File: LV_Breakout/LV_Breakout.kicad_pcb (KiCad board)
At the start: 2 copper layers, 116.8 x 64.8 mm, 17 parts, among them J1 LOGIC_PWR, J2 GLV_IN, J4 BMS, J5 DAQ, J6 DAQ_AMPSEAL, J7 PWR_AMPSEAL, K1 RAYEX-L90B

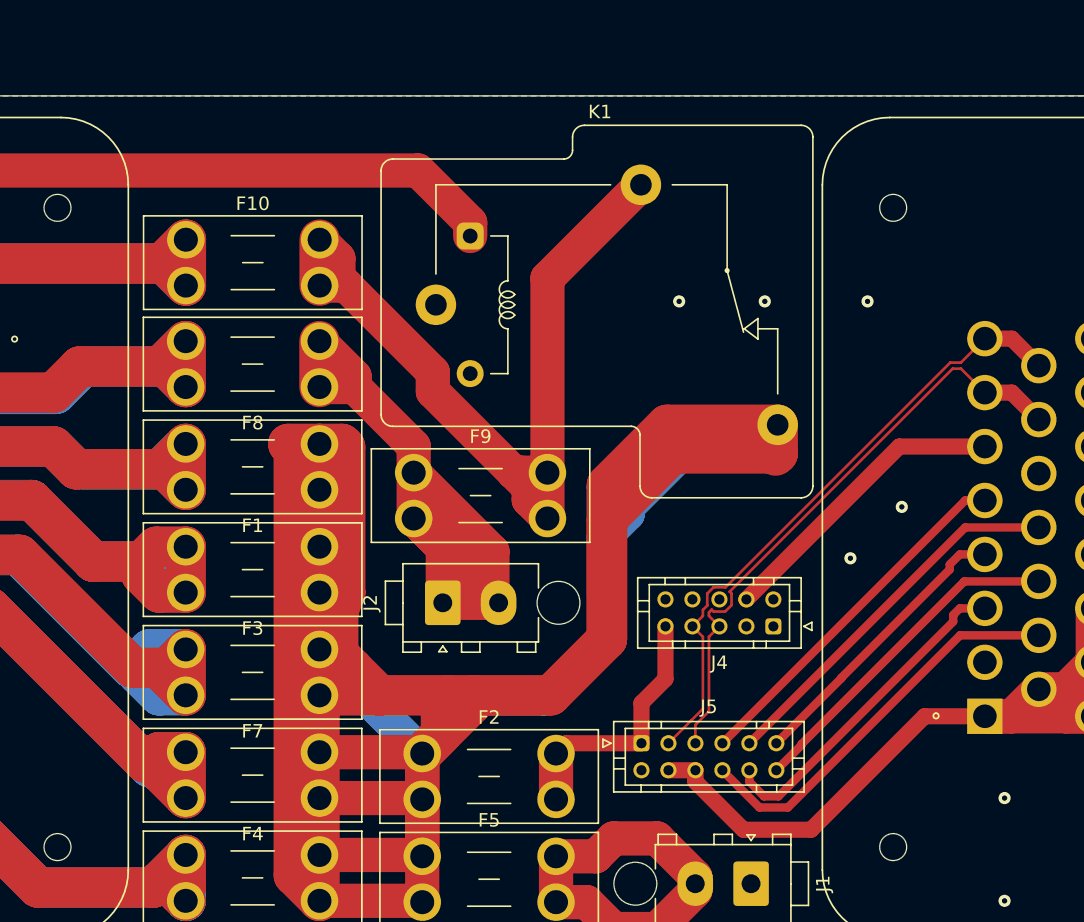
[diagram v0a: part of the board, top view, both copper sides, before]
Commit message: Footprint updates of GLV board, pull the libraries repo please!
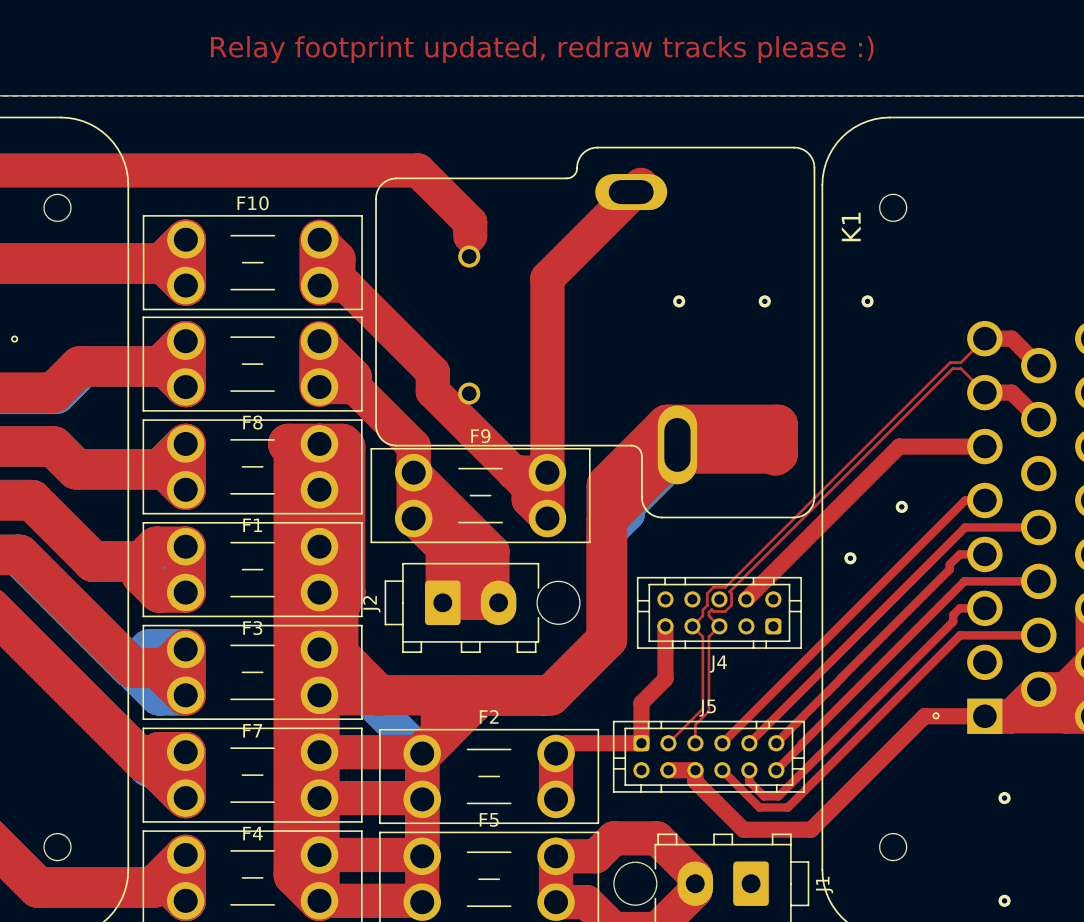
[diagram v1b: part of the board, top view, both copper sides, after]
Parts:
- F1, F10, F2, F3, F4, F5, F6, F7, F8, F9: footprint Fuse:Fuseholder_Blade_Mini_Keystone_3568 -> AERO-footprints:Fuseholder_Blade_Mini_Keystone_3568
- J1, J2: footprint aero_footprint:TE_MATE-N-LOK_1-770866-x_1x02_P4.14mm_Vertical -> AERO-footprints:TE_MATE-N-LOK_1-770866-x_1x02_P4.14mm_Vertical
- J4: footprint Connector_JST:JST_PHD_B10B-PHDSS_2x05_P2.00mm_Vertical -> AERO-footprints:JST_PHD_B10B-PHDSS_2x05_P2.00mm_Vertical
- J5: footprint Connector_JST:JST_PHD_B12B-PHDSS_2x06_P2.00mm_Vertical -> AERO-footprints:JST_PHD_B12B-PHDSS_2x06_P2.00mm_Vertical
- J6, J7: footprint aero_footprint:TE_1-776200-1_23pin_Vertical -> AERO-footprints:TE_1-776200-1_23pin_Vertical
- K1: value RAYEX-L90B -> T9VV1K15-12S; footprint Relay_THT:Relay_SPST_RAYEX-L90B -> AERO-footprints:RELAY_T9VV1K15-12S
- moved K1 14.5 mm to (194.6, 22.9), turned to 270 degrees
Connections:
- J4 pad 1: (no net) -> /USB_GND
- J4 pad 2: (no net) -> /USB+
- J4 pad 3: (no net) -> /USB-
- J4 pad 6: (no net) -> /USB_5V
- J4 pad 8: (no net) -> Net-(J4-Pad8)
- J6 pad 13: (no net) -> Net-(J6-Pad13)
- J6 pad 2: (no net) -> /SENSOR_7
- J7 pad 1: (no net) -> Net-(J7-Pad1)
- J7 pad 17: (no net) -> Net-(J7-Pad17)
- J7 pad 18: (no net) -> Net-(J7-Pad18)
- J7 pad 7: (no net) -> Net-(J7-Pad7)
- J7 pad 8: (no net) -> Net-(J7-Pad8)
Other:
- board text added: "Relay footprint updated, redraw tracks please :)"

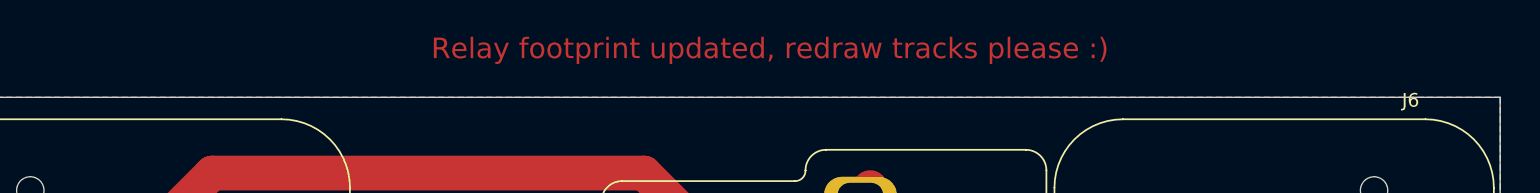
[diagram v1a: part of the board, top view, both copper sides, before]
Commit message: Final fixes to GLV board so it works with HV board
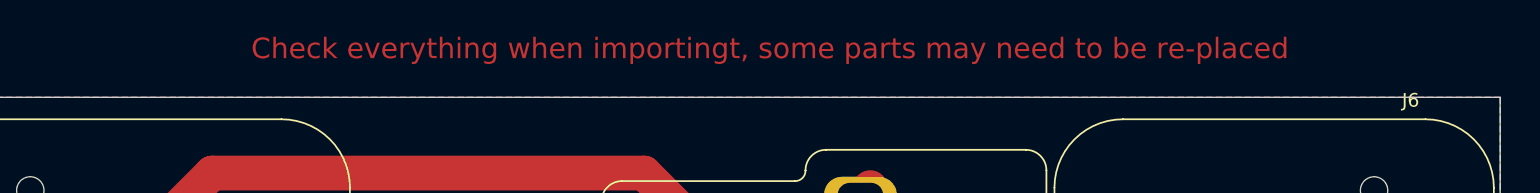
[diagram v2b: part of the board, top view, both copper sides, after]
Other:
- board text added: "Check everything when importingt, some parts may need to be re-placed"
- board text removed: "Relay footprint updated, redraw tracks please :)"

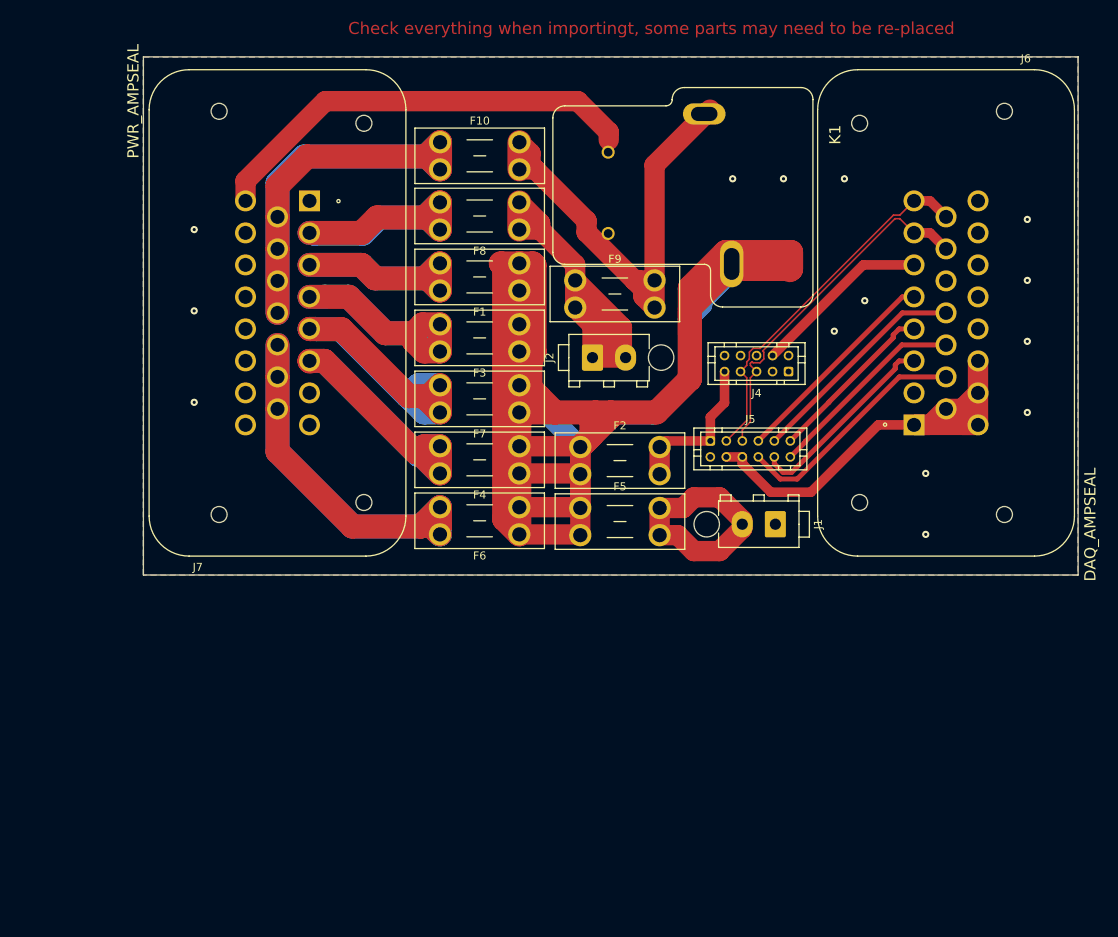
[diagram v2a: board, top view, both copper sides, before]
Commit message: LVPDU schem and pcb
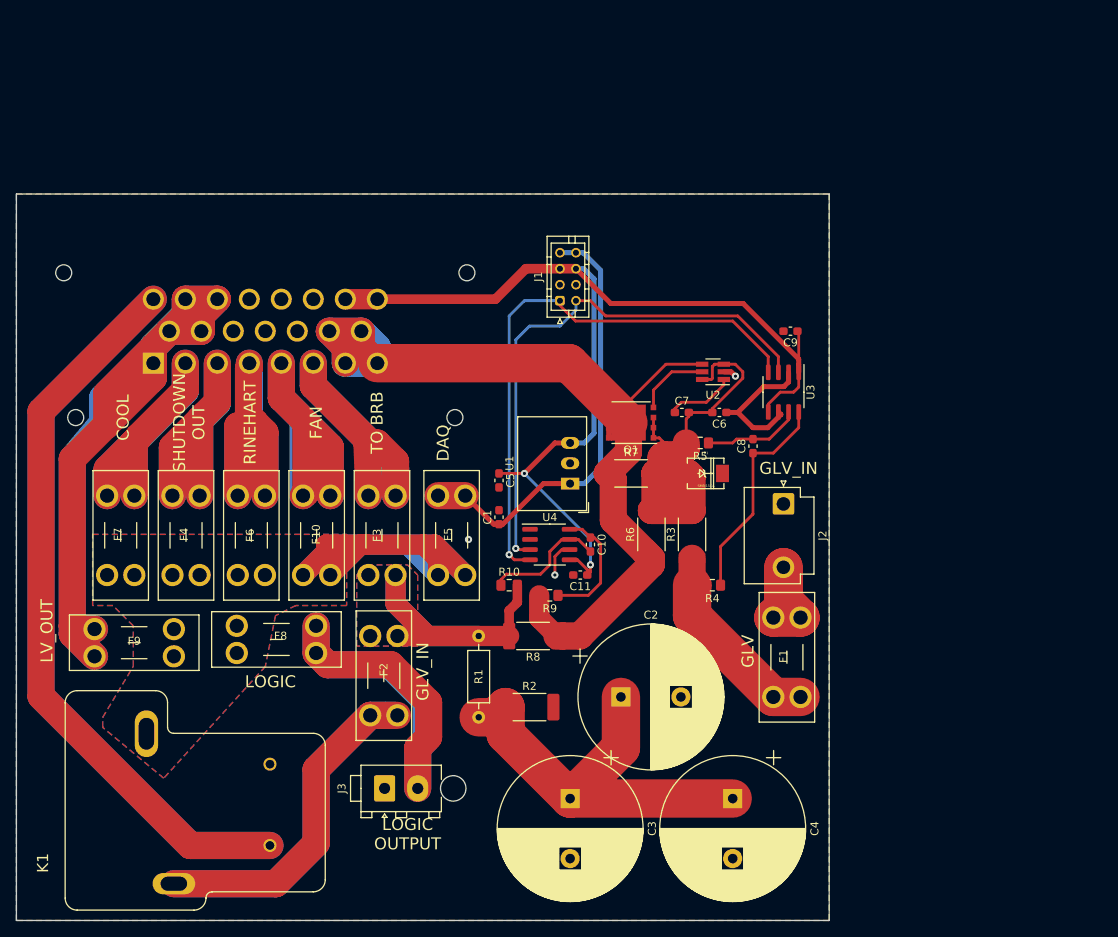
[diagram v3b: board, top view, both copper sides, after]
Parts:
- removed J5: DAQ, AERO-footprints:JST_PHD_B12B-PHDSS_2x06_P2.00mm_Vertical
- removed J6: DAQ_AMPSEAL, AERO-footprints:TE_1-776200-1_23pin_Vertical
- removed J7: PWR_AMPSEAL, AERO-footprints:TE_1-776200-1_23pin_Vertical
- added C1: 1u, Capacitor_SMD:C_0603_1608Metric_Pad1.05x0.95mm_HandSolder, F.Cu at (168.9, 63.9)
- added C10: 1uF, Capacitor_SMD:C_0603_1608Metric_Pad1.05x0.95mm_HandSolder, F.Cu at (180.3, 67.3)
- added C11: 0.1uF, Capacitor_SMD:C_0603_1608Metric_Pad1.05x0.95mm_HandSolder, F.Cu at (179.1, 71.1)
- added C2: URS1E472MHD, Capacitor_THT:CP_Radial_D18.0mm_P7.50mm, F.Cu at (184.2, 86.4)
- added C3: URS1E472MHD, Capacitor_THT:CP_Radial_D18.0mm_P7.50mm, F.Cu at (177.8, 99.1)
- added C4: URS1E472MHD, Capacitor_THT:CP_Radial_D18.0mm_P7.50mm, F.Cu at (198.1, 99.1)
- added C5: 10u, Capacitor_SMD:C_0603_1608Metric_Pad1.05x0.95mm_HandSolder, F.Cu at (168.9, 59.3)
- added C6: 22nF, Capacitor_SMD:C_0603_1608Metric_Pad1.05x0.95mm_HandSolder, F.Cu at (196.5, 50.8)
- added C7: 0.1uF, Capacitor_SMD:C_0603_1608Metric_Pad1.05x0.95mm_HandSolder, F.Cu at (191.8, 50.8)
- added C8: 1uF, Capacitor_SMD:C_0603_1608Metric_Pad1.05x0.95mm_HandSolder, F.Cu at (200.7, 55.0)
- added C9: 0.1uF, Capacitor_SMD:C_0603_1608Metric_Pad1.05x0.95mm_HandSolder, F.Cu at (205.3, 40.6)
- added D1: SMBJ15CA, AERO_FOOT:DO-214AA, F.Cu at (194.7, 58.4)
- added G***: LOGO, AERO_CUSTOM:AERO_Logo_15x6mm, B.Cu at (195.6, 31.8)
- added J3: TE 1-770872-0, AERO_CUSTOM:TE_MATE-N-LOK_1-770866-x_1x02_P4.14mm_Vertical, F.Cu at (154.6, 97.8)
- added Q1: CSD18563Q5A, Package_SON:VSONP-8-1EP_5x6_P1.27mm, F.Cu at (185.4, 52.1)
- added R1: RR01J2R0TB, Resistor_THT:R_Axial_DIN0207_L6.3mm_D2.5mm_P10.16mm_Horizontal, F.Cu at (166.4, 88.9)
- added R10: 10, Resistor_SMD:R_0805_2012Metric_Pad1.15x1.40mm_HandSolder, F.Cu at (170.2, 72.4)
- added R2: 50M, Resistor_SMD:R_2512_6332Metric_Pad1.52x3.35mm_HandSolder, F.Cu at (172.7, 87.6)
- added R3: KRL6432E-M-R003-F-T1, Resistor_SMD:R_2512_6332Metric_Pad1.52x3.35mm_HandSolder, F.Cu at (193.0, 66.0)
- added R4: 10, Resistor_SMD:R_0805_2012Metric_Pad1.15x1.40mm_HandSolder, F.Cu at (195.6, 72.4)
- added R5: 10, Resistor_SMD:R_0805_2012Metric_Pad1.15x1.40mm_HandSolder, F.Cu at (194.1, 54.6)
- added R6: 20, Resistor_SMD:R_2512_6332Metric_Pad1.52x3.35mm_HandSolder, F.Cu at (188.0, 66.0)
- added R7: 20, Resistor_SMD:R_2512_6332Metric_Pad1.52x3.35mm_HandSolder, F.Cu at (185.4, 58.4)
- added R8: KRL6432E-M-R003-F-T1, Resistor_SMD:R_2512_6332Metric_Pad1.52x3.35mm_HandSolder, F.Cu at (173.2, 78.7)
- added R9: 10, Resistor_SMD:R_0805_2012Metric_Pad1.15x1.40mm_HandSolder, F.Cu at (175.3, 73.7)
- added U1: R-78E5.0-0.5, Converter_DCDC:Converter_DCDC_RECOM_R-78E-0.5_THT, F.Cu at (177.8, 59.7)
- added U2: LM74700QDBVTQ1, Package_TO_SOT_SMD:SOT-23-6_Handsoldering, F.Cu at (195.7, 45.7)
- added U3: INA219AIDR, Package_SO:SOIC-8_3.9x4.9mm_P1.27mm, F.Cu at (204.5, 48.3)
- added U4: INA219AIDR, Package_SO:SOIC-8_3.9x4.9mm_P1.27mm, F.Cu at (175.3, 67.3)
- F1: value SHUTDOWN -> 3568 Mini Blade; footprint AERO-footprints:Fuseholder_Blade_Mini_Keystone_3568 -> AERO_FOOT:Fuseholder_Blade_Mini_Keystone_3568
- F10: value DCDC -> 3568 Mini Blade; footprint AERO-footprints:Fuseholder_Blade_Mini_Keystone_3568 -> AERO_FOOT:Fuseholder_Blade_Mini_Keystone_3568
- F2: value BMS -> 3568 Mini Blade; footprint AERO-footprints:Fuseholder_Blade_Mini_Keystone_3568 -> AERO_FOOT:Fuseholder_Blade_Mini_Keystone_3568
- F3: value RINEHART -> 3568 Mini Blade; footprint AERO-footprints:Fuseholder_Blade_Mini_Keystone_3568 -> AERO_FOOT:Fuseholder_Blade_Mini_Keystone_3568
- F4: value COOL -> 3568 Mini Blade; footprint AERO-footprints:Fuseholder_Blade_Mini_Keystone_3568 -> AERO_FOOT:Fuseholder_Blade_Mini_Keystone_3568
- F5: value LOGIC -> 3568 Mini Blade; footprint AERO-footprints:Fuseholder_Blade_Mini_Keystone_3568 -> AERO_FOOT:Fuseholder_Blade_Mini_Keystone_3568
- F6: value LV PWR -> 3568 Mini Blade; footprint AERO-footprints:Fuseholder_Blade_Mini_Keystone_3568 -> AERO_FOOT:Fuseholder_Blade_Mini_Keystone_3568
- F7: value FAN -> 3568 Mini Blade; footprint AERO-footprints:Fuseholder_Blade_Mini_Keystone_3568 -> AERO_FOOT:Fuseholder_Blade_Mini_Keystone_3568
- F8: value BRB -> 3568 Mini Blade; footprint AERO-footprints:Fuseholder_Blade_Mini_Keystone_3568 -> AERO_FOOT:Fuseholder_Blade_Mini_Keystone_3568
- F9: value Main GLV -> 3568 Mini Blade; footprint AERO-footprints:Fuseholder_Blade_Mini_Keystone_3568 -> AERO_FOOT:Fuseholder_Blade_Mini_Keystone_3568
- J1: value LOGIC_PWR -> B10B-PHDSS(LF)(SN); footprint AERO-footprints:TE_MATE-N-LOK_1-770866-x_1x02_P4.14mm_Vertical -> Connector_JST:JST_PHD_B8B-PHDSS_2x04_P2.00mm_Vertical
- J2: value GLV_IN -> DF22-2P-7.92DSA(05); footprint AERO-footprints:TE_MATE-N-LOK_1-770866-x_1x02_P4.14mm_Vertical -> Connector_JST:JST_VH_B2P3-VH_1x02_P7.92mm_Vertical
- J4: value BMS -> TE 776228-1; footprint AERO-footprints:JST_PHD_B10B-PHDSS_2x05_P2.00mm_Vertical -> AERO_CUSTOM:TE_1-776200-1_23pin_Vertical; moved to B.Cu
- K1: footprint AERO-footprints:RELAY_T9VV1K15-12S -> AERO_FOOT:RELAY_T9VV1K15-12S
- moved K1 102.0 mm to (128.3, 100.3), turned to 90 degrees
- moved F9 68.7 mm to (128.3, 81.3), turned to 180 degrees
- moved J4 65.6 mm to (139.7, 40.6), turned to 0 degrees
- moved F8 60.8 mm to (136.1, 77.5), turned to 0 degrees
- moved F1 59.9 mm to (203.2, 86.4), turned to 90 degrees
- moved F10 56.7 mm to (144.4, 71.1), turned to 90 degrees
- moved F7 55.4 mm to (119.9, 71.1), turned to 90 degrees
- moved F4 45.2 mm to (128.1, 71.1), turned to 90 degrees
- moved J1 38.8 mm to (176.5, 36.8), turned to 90 degrees
- moved F6 35.6 mm to (136.3, 71.1), turned to 90 degrees
- moved F2 32.9 mm to (156.2, 78.7), turned to 270 degrees
- moved J2 30.1 mm to (204.5, 62.2), turned to 270 degrees
- moved F3 23.7 mm to (156.0, 61.2), turned to 270 degrees
- moved F5 19.7 mm to (161.3, 71.1), turned to 90 degrees
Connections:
- F1 pad 1: +12V -> /GLV_COMB/VBATT
- F1 pad 2: /SHUTDOWN_OUT -> /BATT_IN
- F10 pad 1: /DCDC_IN -> +12V
- F10 pad 2: Net-(F10-Pad2) -> /FAN_PWR
- F2 pad 1: +12V -> /GLV_IN
- F2 pad 2: /BMS+DAQ_PWR -> Net-(F2-Pad2)
- F3 pad 1: +12V -> /TO_BRB
- F3 pad 2: /RINE_PWR -> /GLV_IN
- F4 pad 2: /COOL_PWR -> /SHUTDOWN_OUT
- F5 pad 2: Net-(F5-Pad2) -> /DAQ_PWR
- F6 pad 2: /LV_PWR -> /RINE_PWR
- F7 pad 2: /FAN_PWR -> /COOL_PWR
- F8 pad 1: /GLV_IN -> +12V
- F8 pad 2: /TO_BRB -> /LOGIC
- F9 pad 1: /GLV_IN -> +12V
- F9 pad 2: Net-(F10-Pad2) -> /LV_PWR
- J1 pad 1: GND -> /SCL
- J1 pad 2: Net-(F5-Pad2) -> /SDA
- J2 pad 1: /GLV_IN -> GND
- J2 pad 2: /GLV_IN -> /BATT_IN
- J4 pad 1: /USB_GND -> /LV_PWR
- J4 pad 10: GND -> /LV_PWR
- J4 pad 2: /USB+ -> /COOL_PWR
- J4 pad 3: /USB- -> /SHUTDOWN_OUT
- J4 pad 4: /BMS_FAULT -> /RINE_PWR
- J4 pad 5: /CAN+ -> /FAN_PWR
- J4 pad 6: /USB_5V -> /TO_BRB
- J4 pad 7: /CAN- -> /DCDC_IN
- J4 pad 8: Net-(J4-Pad8) -> /DCDC_IN
- J4 pad 9: /BMS+DAQ_PWR -> /LV_PWR
- K1 pad 3: Net-(F10-Pad2) -> Net-(F2-Pad2)
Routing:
- net +12V: track 351.0 -> 78.9 mm
- net /FROM_BRB: track 54.6 -> 183.6 mm
- net Net-(F2-Pad2): track 0.00 -> 83.8 mm
- net +5V: track 59.8 -> 135.0 mm, vias 0 -> 2
- net /LV_PWR: track 89.9 -> 164.8 mm
- net /SCL: track 0.00 -> 71.1 mm, vias 0 -> 1
- net /SDA: track 0.00 -> 68.3 mm, vias 0 -> 1
- net Net-(F10-Pad2): track 63.1 -> 0.00 mm
- net /LOGIC: track 0.00 -> 62.3 mm
- net /GLV_COMB/VBATT_CUROUT: track 0.00 -> 59.1 mm
- net /DAQ_PWR: track 0.00 -> 55.4 mm
- net /VCAP_AB: track 0.00 -> 54.3 mm
- net /CAN-: track 46.2 -> 0.00 mm
- net /CAN+: track 45.2 -> 0.00 mm
- net /DCDC_IN: track 85.4 -> 122.0 mm
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- added copper zone on B.Cu, net +12V
- added copper zone on F.Cu, net +12V
- added copper zone on B.Cu, net /GLV_IN
- added copper zone on F.Cu, net /GLV_IN
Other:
- board size 116.8 x 64.8 mm -> 101.6 x 90.8 mm
- net class PWR: trace_width 3 -> 3.4; via_dia 5 -> 4
- board text added: "COOL"
- board text added: "DAQ"
- board text added: "FAN"
- board text added: "GLV"
- board text added: "GLV_IN"
- board text added: "LOGIC"
- board text added: "LOGIC OUTPUT"
- board text added: "LV_OUT"
- board text added: "RINEHART"
- board text added: "SHUTDOWN OUT"
- board text added: "TO BRB"
- board text removed: "Check everything when importingt, some parts may need to be re-placed"

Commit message: second revision
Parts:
- C1, C5: moved to B.Cu
- J3: footprint AERO_CUSTOM:TE_MATE-N-LOK_1-770866-x_1x02_P4.14mm_Vertical -> AERO_CUSTOM:TE_MATE-N-LOK_1-770870-x_1x03_P4.14mm_Vertical
- R3, R8: footprint Resistor_SMD:R_2512_6332Metric_Pad1.52x3.35mm_HandSolder -> AERO_FOOT:KRL6432E-M-R003-F-T1
- moved C1 12.3 mm to (181.2, 62.9), turned to 0 degrees
- moved C5 12.3 mm to (177.2, 50.2), turned to 180 degrees
- moved J3 10.2 mm to (154.9, 108.0), turned to 180 degrees
- moved R9 6.35 mm to (180.3, 69.8), turned to 0 degrees
- moved R4 4.32 mm to (198.8, 75.3), turned to 270 degrees
- moved C11 3.64 mm to (175.7, 72.4)
- moved C10 2.84 mm to (177.8, 66.0)
- moved C7 2.84 mm to (194.3, 49.5), turned to 180 degrees
- moved R1 2.54 mm to (163.8, 88.9)
- moved U4 2.47 mm to (172.8, 67.3)
- moved C6 2.24 mm to (194.3, 51.4)
- moved R8 1.83 mm to (171.4, 79.4)
- moved G*** 1.42 mm to (196.8, 31.1)
- moved U2 1.35 mm to (194.3, 45.7)
- moved R3 1.27 mm to (194.3, 66.0)
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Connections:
- J3 pad 2: /LOGIC -> /FROM_BRB
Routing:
- net /LV_PWR: track 164.8 -> 0.00 mm
- net /DCDC_IN: track 122.0 -> 8.50 mm
- net +12V: track 78.9 -> 0.00 mm
- net /FROM_BRB: track 183.6 -> 122.6 mm
- net /GLV_COMB/VBATT_CUROUT: track 59.1 -> 4.28 mm
- net /VCAP_AB: track 54.3 -> 0.00 mm
- net Net-(F2-Pad2): track 83.8 -> 41.3 mm
- net /GLV_IN: track 49.5 -> 10.5 mm
- net /LOGIC: track 62.3 -> 27.0 mm
- net /BATT_IN: track 17.4 -> 0.00 mm
- net /RINE_PWR: track 56.0 -> 40.4 mm
- net /FAN_PWR: track 57.0 -> 42.2 mm
- net GND: track 24.1 -> 9.33 mm, vias 3 -> 9
- net /SHUTDOWN_OUT: track 57.4 -> 44.6 mm
- net /TO_BRB: track 56.0 -> 45.6 mm
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- added copper zone on F.Cu, net /BATT_IN
- added copper zone on F.Cu, net /DCDC_IN
- added copper zone on F.Cu, net /GLV_COMB/VBATT_CUROUT
- added copper zone on B.Cu, net /LV_PWR
- added copper zone on F.Cu, net /LV_PWR
- added copper zone on F.Cu, net /VCAP_AB
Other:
- board text removed: "LOGIC OUTPUT"

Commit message: Updated PCB Layout
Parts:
- moved F1 5.92 mm to (200.2, 91.4)
- moved C4 5.18 mm to (193.0, 100.1)
- moved R3 4.76 mm to (192.0, 70.2)
- moved C3 4.57 mm to (173.2, 99.1)
- moved C2 3.84 mm to (180.3, 86.9)
- moved J2 3.31 mm to (201.7, 64.0)
- moved R4 3.29 mm to (195.6, 76.2), turned to 180 degrees
- moved R2 3.14 mm to (169.7, 88.4), turned to 90 degrees
- moved R6 2.58 mm to (187.5, 63.5), turned to 0 degrees
- moved G*** 1.37 mm to (196.1, 30.0)
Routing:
- net +5V: track 138.2 -> 147.0 mm
- net /SCL: track 68.5 -> 76.7 mm
- net /SDA: track 64.6 -> 70.6 mm
- net Net-(C8-Pad1): track 28.7 -> 31.5 mm
- net /GLV_COMB/VBATT: track 30.0 -> 28.2 mm
- net GND: vias 9 -> 12
- net /LV_PWR: vias 0 -> 4
- added copper zone on B.Cu, net /BATT_IN
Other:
- board text added: "LVPDU G.Spearing 20.0228"
- board text added: "WATER"
- board text removed: "COOL"
